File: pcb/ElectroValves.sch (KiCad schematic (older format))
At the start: 39 parts, among them P2 Conn_01x04_Female, Q1 PN2222, Q2 PN2222, U11 AQH3213AX, U12 AQH3213AX, U3 TLP240D, U4 TLP240D, U5 TLP240D, U6 TLP240D, U7 TLP240D, U8 TLP240D

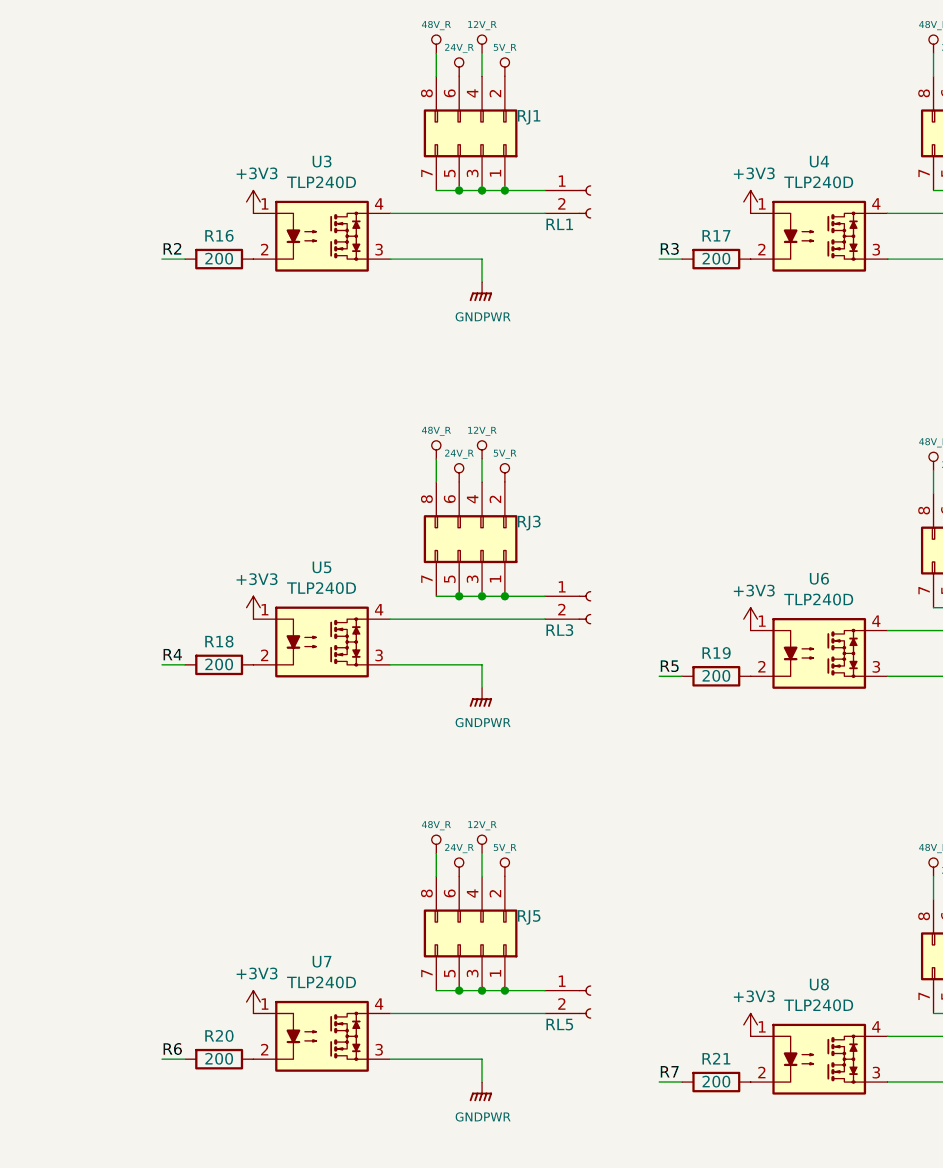
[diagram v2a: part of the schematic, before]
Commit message: Solved connection problem with XCL214B333DR and it was added 3 leds to the board
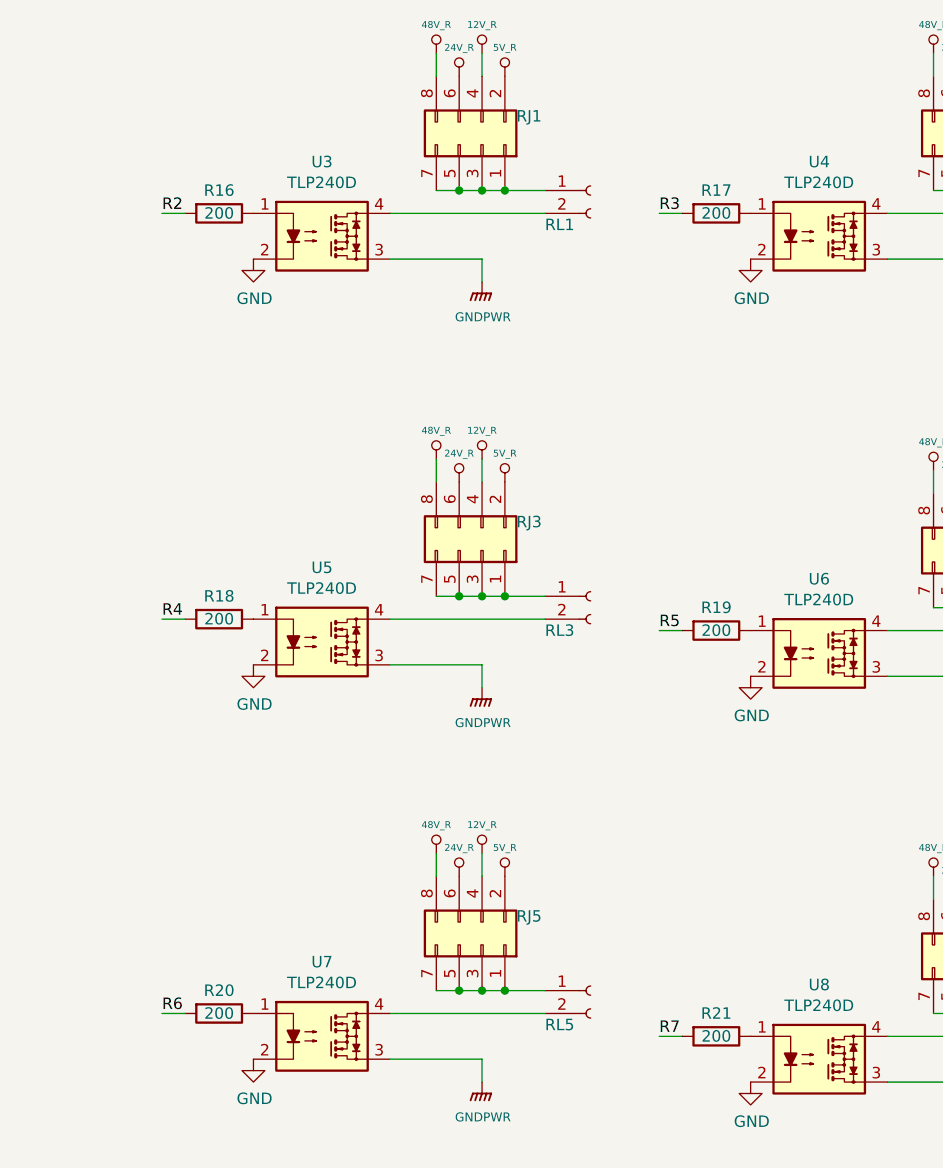
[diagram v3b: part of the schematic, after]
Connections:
- net +3V3: no longer U3.1, U4.1, U5.1, U6.1, U7.1, U8.1
- net GND: now also U3.2, U4.2, U5.2, U6.2, U7.2, U8.2
- net at R16.1: now also U3.1; no longer U3.2
- net at R17.1: now also U4.1; no longer U4.2
- net at R18.1: now also U5.1; no longer U5.2
- net at R19.1: now also U6.1; no longer U6.2
- net at R20.1: now also U7.1; no longer U7.2
- net at R21.1: now also U8.1; no longer U8.2
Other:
- moved on the sheet: R16, R17, R18, R19, R20, R21
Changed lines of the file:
@@
 L Device:R R16
 U 1 1 5E903E97
-P 2400 1800
-F 0 "R16" V 2300 1800 50  0000 C CNN
-F 1 "200" V 2400 1800 50  0000 C CNN
-F 2 "Resistor_SMD:R_0402_1005Metric" V 2330 1800 50  0001 C CNN
-F 3 "~" H 2400 1800 50  0001 C CNN
-	1    2400 1800
+P 2400 1600
+F 0 "R16" V 2300 1600 50  0000 C CNN
+F 1 "200" V 2400 1600 50  0000 C CNN
+F 2 "Resistor_SMD:R_0402_1005Metric" V 2330 1600 50  0001 C CNN
+F 3 "~" H 2400 1600 50  0001 C CNN
+	1    2400 1600
 	0    1    1    0
 $EndComp
@@
 L Device:R R17
 U 1 1 5E904242
-P 4575 1800
-F 0 "R17" V 4475 1800 50  0000 C CNN
-F 1 "200" V 4575 1800 50  0000 C CNN
-F 2 "Resistor_SMD:R_0402_1005Metric" V 4505 1800 50  0001 C CNN
-F 3 "~" H 4575 1800 50  0001 C CNN
-	1    4575 1800
+P 4575 1600
+F 0 "R17" V 4475 1600 50  0000 C CNN
+F 1 "200" V 4575 1600 50  0000 C CNN
+F 2 "Resistor_SMD:R_0402_1005Metric" V 4505 1600 50  0001 C CNN
+F 3 "~" H 4575 1600 50  0001 C CNN
+	1    4575 1600
 	0    1    1    0
 $EndComp
@@
 L Device:R R18
 U 1 1 5E905901
-P 2400 3575
-F 0 "R18" V 2300 3575 50  0000 C CNN
-F 1 "200" V 2400 3575 50  0000 C CNN
-F 2 "Resistor_SMD:R_0402_1005Metric" V 2330 3575 50  0001 C CNN
-F 3 "~" H 2400 3575 50  0001 C CNN
-	1    2400 3575
+P 2400 3375
+F 0 "R18" V 2300 3375 50  0000 C CNN
+F 1 "200" V 2400 3375 50  0000 C CNN
+F 2 "Resistor_SMD:R_0402_1005Metric" V 2330 3375 50  0001 C CNN
+F 3 "~" H 2400 3375 50  0001 C CNN
+	1    2400 3375
 	0    1    1    0
 $EndComp
@@
 L Device:R R19
 U 1 1 5E906E93
-P 4575 3625
-F 0 "R19" V 4475 3625 50  0000 C CNN
-F 1 "200" V 4575 3625 50  0000 C CNN
-F 2 "Resistor_SMD:R_0402_1005Metric" V 4505 3625 50  0001 C CNN
-F 3 "~" H 4575 3625 50  0001 C CNN
-	1    4575 3625
+P 4575 3425
+F 0 "R19" V 4475 3425 50  0000 C CNN
+F 1 "200" V 4575 3425 50  0000 C CNN
+F 2 "Resistor_SMD:R_0402_1005Metric" V 4505 3425 50  0001 C CNN
+F 3 "~" H 4575 3425 50  0001 C CNN
+	1    4575 3425
 	0    1    1    0
 $EndComp
@@
 L Device:R R20
 U 1 1 5E90842A
-P 2400 5300
-F 0 "R20" V 2300 5300 50  0000 C CNN
-F 1 "200" V 2400 5300 50  0000 C CNN
-F 2 "Resistor_SMD:R_0402_1005Metric" V 2330 5300 50  0001 C CNN
-F 3 "~" H 2400 5300 50  0001 C CNN
-	1    2400 5300
+P 2400 5100
+F 0 "R20" V 2300 5100 50  0000 C CNN
+F 1 "200" V 2400 5100 50  0000 C CNN
+F 2 "Resistor_SMD:R_0402_1005Metric" V 2330 5100 50  0001 C CNN
+F 3 "~" H 2400 5100 50  0001 C CNN
+	1    2400 5100
 	0    1    1    0
 $EndComp
@@
 L Device:R R21
 U 1 1 5E909A7C
-P 4575 5400
-F 0 "R21" V 4475 5400 50  0000 C CNN
-F 1 "200" V 4575 5400 50  0000 C CNN
-F 2 "Resistor_SMD:R_0402_1005Metric" V 4505 5400 50  0001 C CNN
-F 3 "~" H 4575 5400 50  0001 C CNN
-	1    4575 5400
+P 4575 5200
+F 0 "R21" V 4475 5200 50  0000 C CNN
+F 1 "200" V 4575 5200 50  0000 C CNN
+F 2 "Resistor_SMD:R_0402_1005Metric" V 4505 5200 50  0001 C CNN
+F 3 "~" H 4575 5200 50  0001 C CNN
+	1    4575 5200
 	0    1    1    0
 $EndComp
@@
 Wire Wire Line
 	6950 3000 7050 3000
-Text Label 2150 1800 0    50   ~ 0
+Text Label 2150 1600 0    50   ~ 0
 R2
 Wire Wire Line
-	2150 1800 2250 1800
-Wire Wire Line
-	4325 3625 4425 3625
-Text Label 4325 3625 0    50   ~ 0
+	2150 1600 2250 1600
+Wire Wire Line
+	4325 3425 4425 3425
+Text Label 4325 3425 0    50   ~ 0
 R5
 Wire Wire Line
-	2150 3575 2250 3575
-Text Label 2150 3575 0    50   ~ 0
+	2150 3375 2250 3375
+Text Label 2150 3375 0    50   ~ 0
 R4
 Wire Wire Line
-	4325 1800 4425 1800
-Text Label 4325 1800 0    50   ~ 0
+	4325 1600 4425 1600
+Text Label 4325 1600 0    50   ~ 0
 R3
 NoConn ~ 9750 3000
@@
 	10150 1050 10775 1050
 Connection ~ 10150 1050
-Text Label 2150 5300 0    50   ~ 0
+Text Label 2150 5100 0    50   ~ 0
 R6
 Wire Wire Line
-	2150 5300 2250 5300
-Wire Wire Line
-	4325 5400 4425 5400
-Text Label 4325 5400 0    50   ~ 0
+	2150 5100 2250 5100
+Wire Wire Line
+	4325 5200 4425 5200
+Text Label 4325 5200 0    50   ~ 0
 R7
 $Comp
@@
 F 3 "~" H 4025 3275 50  0001 C CNN
 	1    4025 3275
-	1    0    0    -1
-$EndComp
-$Comp
-L power:+3V3 #PWR0146
-U 1 1 5EB7FD99
-P 2550 1600
-F 0 "#PWR0146" H 2550 1450 50  0001 C CNN
-F 1 "+3V3" H 2565 1773 50  0000 C CNN
-F 2 "" H 2550 1600 50  0001 C CNN
-F 3 "" H 2550 1600 50  0001 C CNN
-	1    2550 1600
-	1    0    0    -1
-$EndComp
-$Comp
-L power:+3V3 #PWR0173
-U 1 1 5EB8A9DE
-P 4725 5200
-F 0 "#PWR0173" H 4725 5050 50  0001 C CNN
-F 1 "+3V3" H 4740 5373 50  0000 C CNN
-F 2 "" H 4725 5200 50  0001 C CNN
-F 3 "" H 4725 5200 50  0001 C CNN
-	1    4725 5200
-	1    0    0    -1
-$EndComp
-$Comp
-L power:+3V3 #PWR0231
-U 1 1 5EB8B835
-P 2550 3375
-F 0 "#PWR0231" H 2550 3225 50  0001 C CNN
-F 1 "+3V3" H 2565 3548 50  0000 C CNN
-F 2 "" H 2550 3375 50  0001 C CNN
-F 3 "" H 2550 3375 50  0001 C CNN
-	1    2550 3375
-	1    0    0    -1
-$EndComp
-$Comp
-L power:+3V3 #PWR0252
-U 1 1 5EB8C2EA
-P 2550 5100
-F 0 "#PWR0252" H 2550 4950 50  0001 C CNN
-F 1 "+3V3" H 2565 5273 50  0000 C CNN
-F 2 "" H 2550 5100 50  0001 C CNN
-F 3 "" H 2550 5100 50  0001 C CNN
-	1    2550 5100
-	1    0    0    -1
-$EndComp
-$Comp
-L power:+3V3 #PWR0253
-U 1 1 5EB90B87
-P 4725 3425
-F 0 "#PWR0253" H 4725 3275 50  0001 C CNN
-F 1 "+3V3" H 4740 3598 50  0000 C CNN
-F 2 "" H 4725 3425 50  0001 C CNN
-F 3 "" H 4725 3425 50  0001 C CNN
-	1    4725 3425
-	1    0    0    -1
-$EndComp
-$Comp
-L power:+3V3 #PWR0254
-U 1 1 5EBA06EE
-P 4725 1600
-F 0 "#PWR0254" H 4725 1450 50  0001 C CNN
-F 1 "+3V3" H 4740 1773 50  0000 C CNN
-F 2 "" H 4725 1600 50  0001 C CNN
-F 3 "" H 4725 1600 50  0001 C CNN
-	1    4725 1600
 	1    0    0    -1
 $EndComp
@@
 	1    0    0    -1
 $EndComp
+$Comp
+L power:GND #PWR0122
+U 1 1 5ECF0D40
+P 2550 1800
+F 0 "#PWR0122" H 2550 1550 50  0001 C CNN
+F 1 "GND" H 2555 1627 50  0000 C CNN
+F 2 "" H 2550 1800 50  0001 C CNN
+F 3 "" H 2550 1800 50  0001 C CNN
+	1    2550 1800
+	1    0    0    -1
+$EndComp
+$Comp
+L power:GND #PWR0126
+U 1 1 5ECF18FB
+P 2550 3575
+F 0 "#PWR0126" H 2550 3325 50  0001 C CNN
+F 1 "GND" H 2555 3402 50  0000 C CNN
+F 2 "" H 2550 3575 50  0001 C CNN
+F 3 "" H 2550 3575 50  0001 C CNN
+	1    2550 3575
+	1    0    0    -1
+$EndComp
+$Comp
+L power:GND #PWR0146
+U 1 1 5ECF244B
+P 2550 5300
+F 0 "#PWR0146" H 2550 5050 50  0001 C CNN
+F 1 "GND" H 2555 5127 50  0000 C CNN
+F 2 "" H 2550 5300 50  0001 C CNN
+F 3 "" H 2550 5300 50  0001 C CNN
+	1    2550 5300
+	1    0    0    -1
+$EndComp
+$Comp
+L power:GND #PWR0173
+U 1 1 5ECF2F08
+P 4725 1800
+F 0 "#PWR0173" H 4725 1550 50  0001 C CNN
+F 1 "GND" H 4730 1627 50  0000 C CNN
+F 2 "" H 4725 1800 50  0001 C CNN
+F 3 "" H 4725 1800 50  0001 C CNN
+	1    4725 1800
+	1    0    0    -1
+$EndComp
+$Comp
+L power:GND #PWR0231
+U 1 1 5ECF3900
+P 4725 3625
+F 0 "#PWR0231" H 4725 3375 50  0001 C CNN
+F 1 "GND" H 4730 3452 50  0000 C CNN
+F 2 "" H 4725 3625 50  0001 C CNN
+F 3 "" H 4725 3625 50  0001 C CNN
+	1    4725 3625
+	1    0    0    -1
+$EndComp
+$Comp
+L power:GND #PWR0252
+U 1 1 5ECF43AC
+P 4725 5400
+F 0 "#PWR0252" H 4725 5150 50  0001 C CNN
+F 1 "GND" H 4730 5227 50  0000 C CNN
+F 2 "" H 4725 5400 50  0001 C CNN
+F 3 "" H 4725 5400 50  0001 C CNN
+	1    4725 5400
+	1    0    0    -1
+$EndComp

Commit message: Added two SSR AQH3223AX on schema
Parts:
- added C76, C77: 0.1u 250V, Capacitor_SMD:C_1210_3225Metric, symbol Device:C
- added Q6, Q7: PN2222, SMD:SOT23_Transistor, symbol Transistor_BJT:PN2222A
- added R56, R59: 100 1/2W, Resistor_SMD:R_0612_1632Metric, symbol Device:R
- added R57, R60: 22, Resistor_SMD:R_0402_1005Metric, symbol Device:R
- added R58: 330, Resistor_SMD:R_0402_1005Metric, symbol Device:R
- added R61: 200, Resistor_SMD:R_0402_1005Metric, symbol Device:R
- added RL10, RL9: Conn_01x04_Female, Connector_Phoenix_MSTB:PhoenixContact_MSTBA_2,5_2-G-5,08_1x02_P5.08mm_Horizontal, symbol BarrelConnector:Conn_01x02_Female
- added U19, U20: AQH3223AX, SMD:AQH3223A, symbol AQH3213AX:AQH3223AX
- U11, U12: value AQH3213AX -> AQH3223AX; symbol AQH3213AX:AQH3213AX -> AQH3213AX:AQH3223AX; Digikey 255-6001-1-ND -> 255-6003-1-ND
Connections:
- net +3V3: now also U19.2, U20.2
- net GND: now also Q6.1 (E), Q7.1 (E)
- net LINE: now also RL10.1 (Pin_1), RL9.1 (Pin_1)
- net NEUT: now also C76.2, C77.2, U19.6, U20.6
- new net: R56.1, RL9.2 (Pin_2), U19.8
- new net: C76.1, R56.2
- new net: R59.1, RL10.2 (Pin_2), U20.8
- new net: C77.1, R59.2
- new net: Q6.2 (B), R58.1
- new net: Q6.3 (C), R57.2
- new net: R60.1, U20.1, U20.3, U20.4
- new net: Q7.3 (C), R60.2
- new net: Q7.2 (B), R61.1
- new net: R57.1, U19.1, U19.3, U19.4
- no-connect marks 2 -> 4
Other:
- moved on the sheet: P2

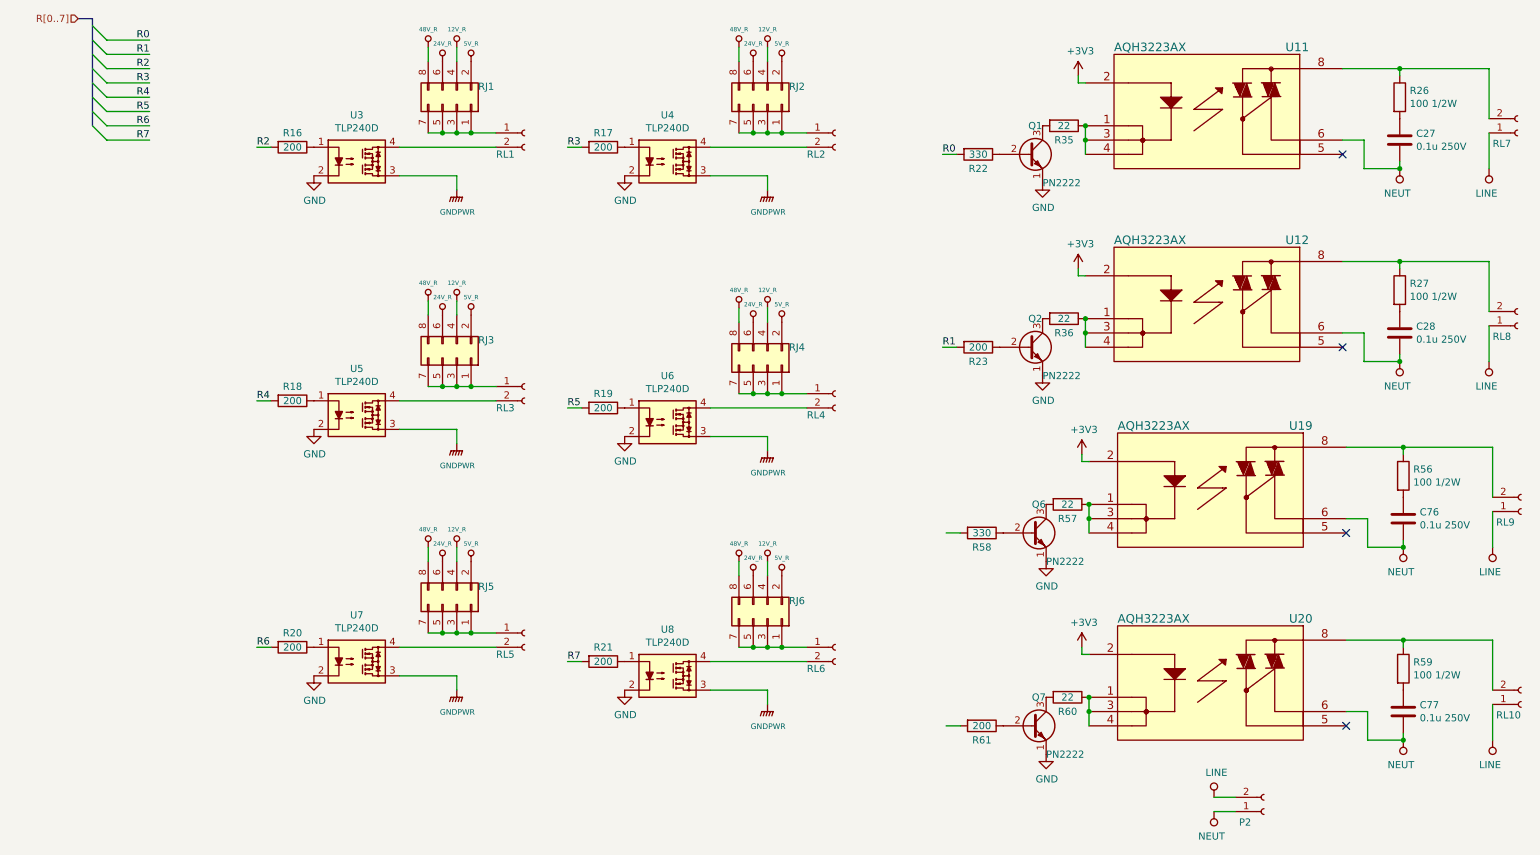
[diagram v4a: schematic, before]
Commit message: Added all connections between STM and AQH3223. added pin header with GPIO from STM
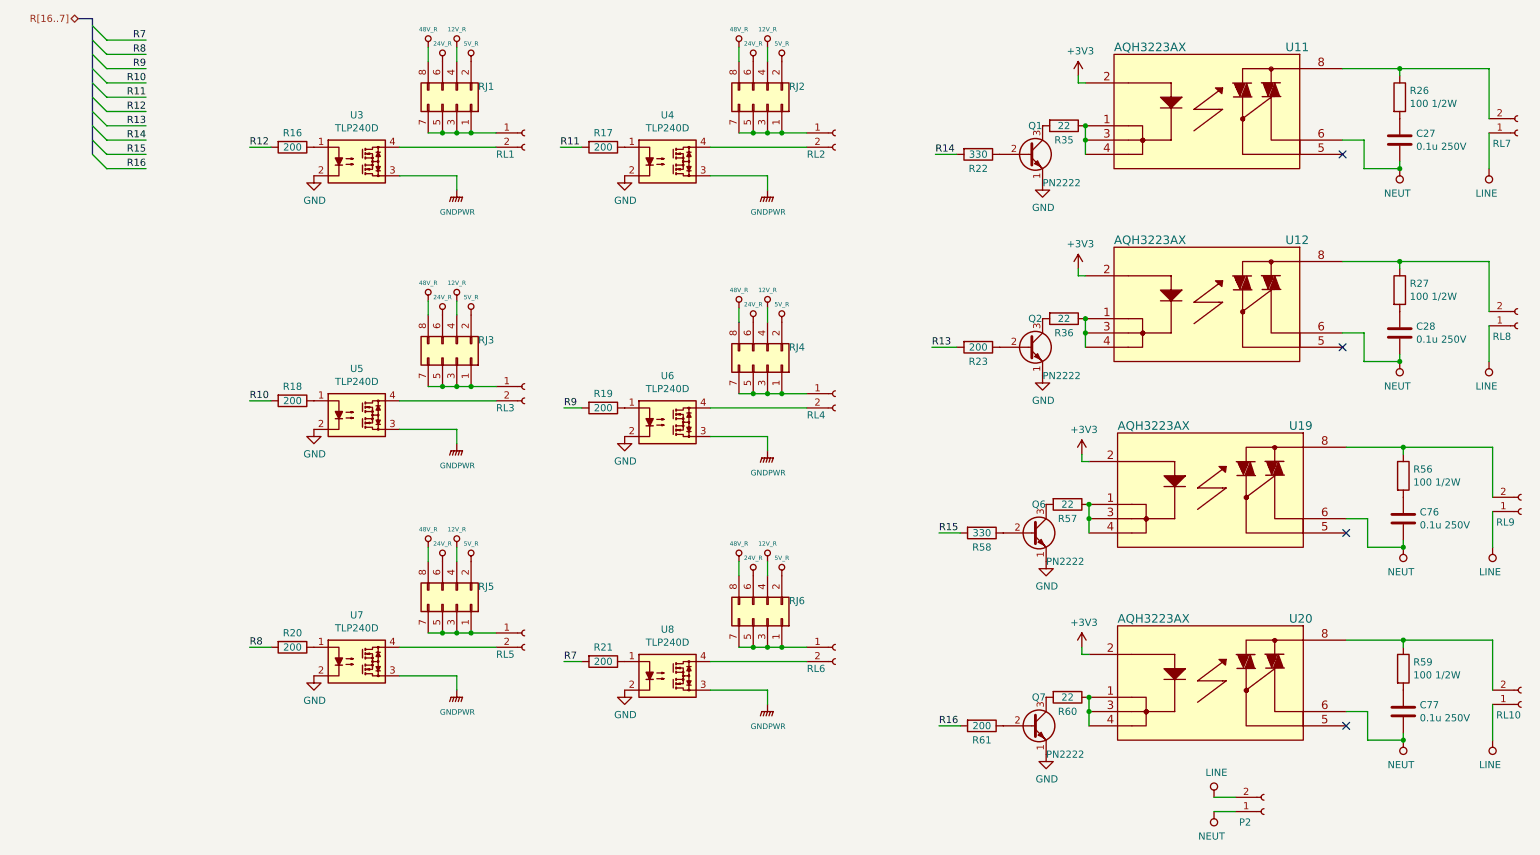
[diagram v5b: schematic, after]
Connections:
- net R15: now reaches R58.2
- net R16: now reaches R61.2
- net R0 renamed R14
- net R1 renamed R13
- net R2 renamed R12
- net R3 renamed R11
- net R4 renamed R10
- net R5 renamed R9
- net R6 renamed R8
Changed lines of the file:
@@
 	0    1    1    0
 $EndComp
-Text Label 6950 1650 0    50   ~ 0
-R0
-Wire Wire Line
-	6950 1650 7050 1650
-Text Label 6950 3000 0    50   ~ 0
-R1
-Wire Wire Line
-	6950 3000 7050 3000
-Text Label 2150 1600 0    50   ~ 0
-R2
-Wire Wire Line
-	2150 1600 2250 1600
-Wire Wire Line
-	4325 3425 4425 3425
-Text Label 4325 3425 0    50   ~ 0
-R5
-Wire Wire Line
-	2150 3375 2250 3375
-Text Label 2150 3375 0    50   ~ 0
-R4
-Wire Wire Line
-	4325 1600 4425 1600
-Text Label 4325 1600 0    50   ~ 0
-R3
+Text Label 6900 1650 0    50   ~ 0
+R14
+Wire Wire Line
+	6900 1650 7050 1650
+Text Label 6875 3000 0    50   ~ 0
+R13
+Wire Wire Line
+	6875 3000 7050 3000
+Text Label 2100 1600 0    50   ~ 0
+R12
+Wire Wire Line
+	2100 1600 2250 1600
+Wire Wire Line
+	4300 3425 4425 3425
+Text Label 4300 3425 0    50   ~ 0
+R9
+Wire Wire Line
+	2100 3375 2250 3375
+Text Label 2100 3375 0    50   ~ 0
+R10
+Wire Wire Line
+	4275 1600 4425 1600
+Text Label 4275 1600 0    50   ~ 0
+R11
 NoConn ~ 9750 3000
 NoConn ~ 9750 1650
@@
 	1    0    0    -1
 $EndComp
-Wire Wire Line
-	1100 850  1400 850
-Text Label 1400 850  2    50   ~ 0
-R0
-Wire Wire Line
-	1100 950  1400 950
-Text Label 1400 950  2    50   ~ 0
-R1
-Wire Wire Line
-	1100 1050 1400 1050
-Text Label 1400 1050 2    50   ~ 0
-R2
-Wire Wire Line
-	1100 1150 1400 1150
-Text Label 1400 1150 2    50   ~ 0
-R3
-Wire Wire Line
-	1100 1250 1400 1250
-Text Label 1400 1250 2    50   ~ 0
-R4
-Wire Wire Line
-	1100 1350 1400 1350
-Text Label 1400 1350 2    50   ~ 0
-R5
-Wire Wire Line
-	1100 1450 1400 1450
-Text Label 1400 1450 2    50   ~ 0
-R6
-Wire Wire Line
-	1100 1550 1400 1550
-Text Label 1400 1550 2    50   ~ 0
-R7
 Entry Wire Line
 	1000 850  1100 950
@@
 Wire Bus Line
 	900  700  1000 700
-Text HLabel 900  700  0    50   Input ~ 0
-R[0..7]
+Text HLabel 900  700  0    50   BiDi ~ 0
+R[16..7]
 $Comp
 L BarrelConnector:Conn_01x02_Female RL2
@@
 	10150 1050 10775 1050
 Connection ~ 10150 1050
-Text Label 2150 5100 0    50   ~ 0
-R6
-Wire Wire Line
-	2150 5100 2250 5100
-Wire Wire Line
-	4325 5200 4425 5200
-Text Label 4325 5200 0    50   ~ 0
+Text Label 2100 5100 0    50   ~ 0
+R8
+Wire Wire Line
+	2100 5100 2250 5100
+Wire Wire Line
+	4300 5200 4425 5200
+Text Label 4300 5200 0    50   ~ 0
 R7
 $Comp
@@
 Connection ~ 10175 5050
 Wire Wire Line
-	6975 4300 7075 4300
-Wire Wire Line
-	6975 5650 7075 5650
+	6925 4300 7075 4300
+Wire Wire Line
+	6925 5650 7075 5650
 NoConn ~ 9775 5650
 NoConn ~ 9775 4300
@@
 	1    0    0    -1
 $EndComp
+Entry Wire Line
+	1000 1550 1100 1650
+Entry Wire Line
+	1000 1650 1100 1750
+Wire Wire Line
+	1100 850  1375 850
+Wire Wire Line
+	1100 950  1375 950
+Wire Wire Line
+	1100 1050 1375 1050
+Wire Wire Line
+	1100 1150 1375 1150
+Wire Wire Line
+	1100 1250 1375 1250
+Wire Wire Line
+	1100 1350 1375 1350
+Wire Wire Line
+	1100 1450 1375 1450
+Wire Wire Line
+	1100 1550 1375 1550
+Wire Wire Line
+	1100 1650 1375 1650
+Wire Wire Line
+	1100 1750 1375 1750
+Text Label 1375 850  2    50   ~ 0
+R7
+Text Label 1375 950  2    50   ~ 0
+R8
+Text Label 1375 1050 2    50   ~ 0
+R9
+Text Label 1375 1150 2    50   ~ 0
+R10
+Text Label 1375 1250 2    50   ~ 0
+R11
+Text Label 1375 1350 2    50   ~ 0
+R12
+Text Label 1375 1450 2    50   ~ 0
+R13
+Text Label 1375 1550 2    50   ~ 0
+R14
+Text Label 1375 1650 2    50   ~ 0
+R15
+Text Label 1375 1750 2    50   ~ 0
+R16
+Text Label 6925 4300 0    50   ~ 0
+R15
+Text Label 6925 5650 0    50   ~ 0
+R16
 Wire Bus Line
-	1000 700  1000 1450
+	1000 700  1000 1650
 $EndSCHEMATC
